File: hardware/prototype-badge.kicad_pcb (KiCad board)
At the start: 2 copper layers, 65 parts, among them J1 GCT4105, J2 E-Ink, Q1 Si1308EDL, SW1 BOOTSEL, SW2 RESET, SW3 User1, SW4 User2, SW5 User3, SW6 User4, SW7 LIGHTPROG, U1 USBLC6-2SC6, U2 AMS1117-3.3, U3 W25Q32JVSS, U4 RP2040, U5 NT3H2111-2211, U6 LMV321, Y1 12MHz

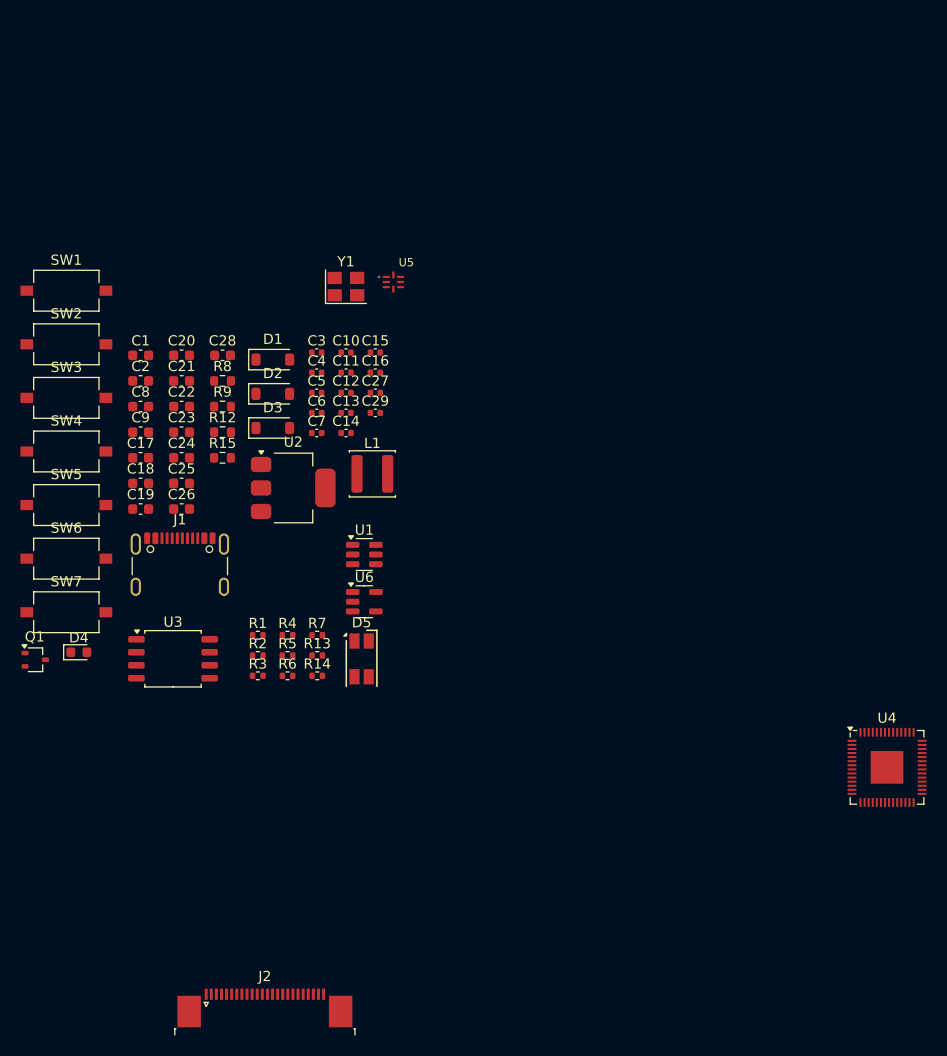
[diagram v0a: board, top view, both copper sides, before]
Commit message: 90% done with pcb, need to add dev pins
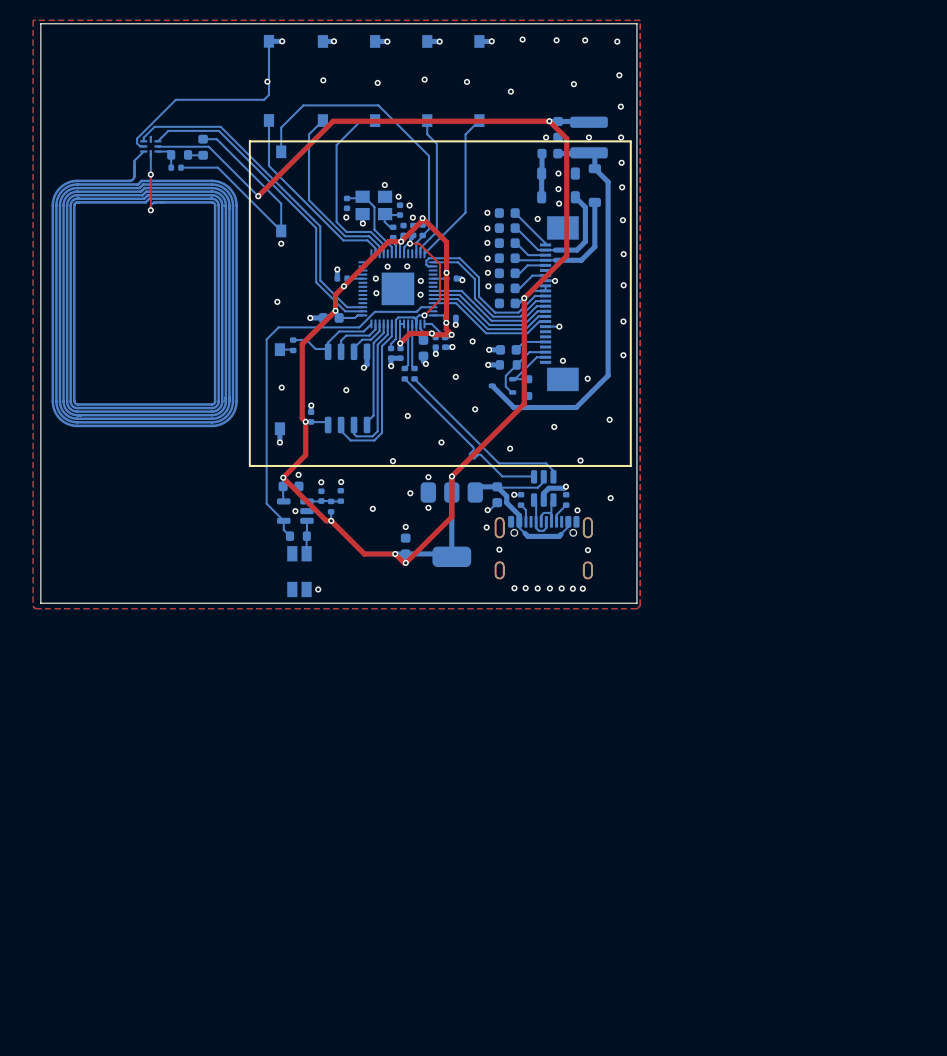
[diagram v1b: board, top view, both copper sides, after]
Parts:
- added L2: 1.755uH, footprints:nfc-coil-2, B.Cu at (141.5, 79.9)
- C1, C10, C11, C12, C13, C14, C15, C16, C17, C18, C19, C2, C20, C21, C22, C23, C24, C25, C26, C27, C28, C29, C3, C4, C5, C6, C7, C8, C9, D1, D2, D3, D4, D5, J1, J2, L1, Q1, R1, R12, R13, R14, R15, R2, R3, R4, R5, R6, R7, R8, R9, SW1, SW2, SW3, SW4, SW5, SW6, SW7, U1, U2, U3, U4, U5, U6, Y1: moved to B.Cu
- moved J2 74.8 mm to (182.1, 79.8), turned to -90 degrees
- moved U4 67.0 mm to (166.3, 78.4)
- moved SW6 61.9 mm to (174.3, 58.0), turned to 90 degrees
- moved SW7 55.7 mm to (153.7, 58.0), turned to 90 degrees
- moved C19 55.3 mm to (182.0, 62.8), turned to -90 degrees
- moved SW5 54.6 mm to (169.2, 58.0), turned to 90 degrees
- moved Q1 53.1 mm to (176.6, 87.9), turned to 180 degrees
- moved D4 51.0 mm to (147.2, 64.5), turned to -90 degrees
- moved C17 50.0 mm to (181.2, 65.2)
- moved SW4 47.2 mm to (164.1, 58.0), turned to 90 degrees
- moved R3 46.5 mm to (168.7, 72.7), turned to -90 degrees
- moved R6 44.7 mm to (165.8, 72.9), turned to 90 degrees
- moved C26 43.1 mm to (177.0, 71.0), turned to 180 degrees
- moved C18 42.2 mm to (177.0, 75.4), turned to 180 degrees
- moved C25 40.5 mm to (177.0, 72.4)
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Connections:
- U5 pad 8: Net-(U5-LA) -> Net-(U5-LB)
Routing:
- net +3.3V: track 0.00 -> 210.3 mm, vias 0 -> 18
- net Earth: track 0.00 -> 74.2 mm, vias 0 -> 106
- net Net-(D3-A): track 0.00 -> 39.4 mm
- net /GPIO28_ADC2_LDR: track 0.00 -> 37.8 mm
- net /I2C_SCL: track 0.00 -> 32.7 mm
- net /I2C_SDA: track 0.00 -> 30.9 mm
- net /RP_RUN: track 0.00 -> 29.9 mm
- net +1V1: track 0.00 -> 21.5 mm, vias 0 -> 2
- net /GPIO13: track 0.00 -> 18.8 mm
- net /GPIO15: track 0.00 -> 18.7 mm
- net VBUS: track 0.00 -> 18.5 mm
- net /USB_D-: track 0.00 -> 17.9 mm
- net /USB_D+: track 0.00 -> 17.9 mm
- net /GPIO14: track 0.00 -> 17.9 mm
- net /SPI_MOSI: track 0.00 -> 16.9 mm
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- added copper zone on B.Cu, net Earth
- added copper zone on F.Cu, net Earth
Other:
- board outline added: 58.4 x 56.8 mm
